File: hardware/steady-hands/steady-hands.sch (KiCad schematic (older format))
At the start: 16 parts, among them J1 SWD, J2 UART, J3 I2C, SW1 SW_Push, SW2 SW_SPDT, U1 STM32F411CEUx

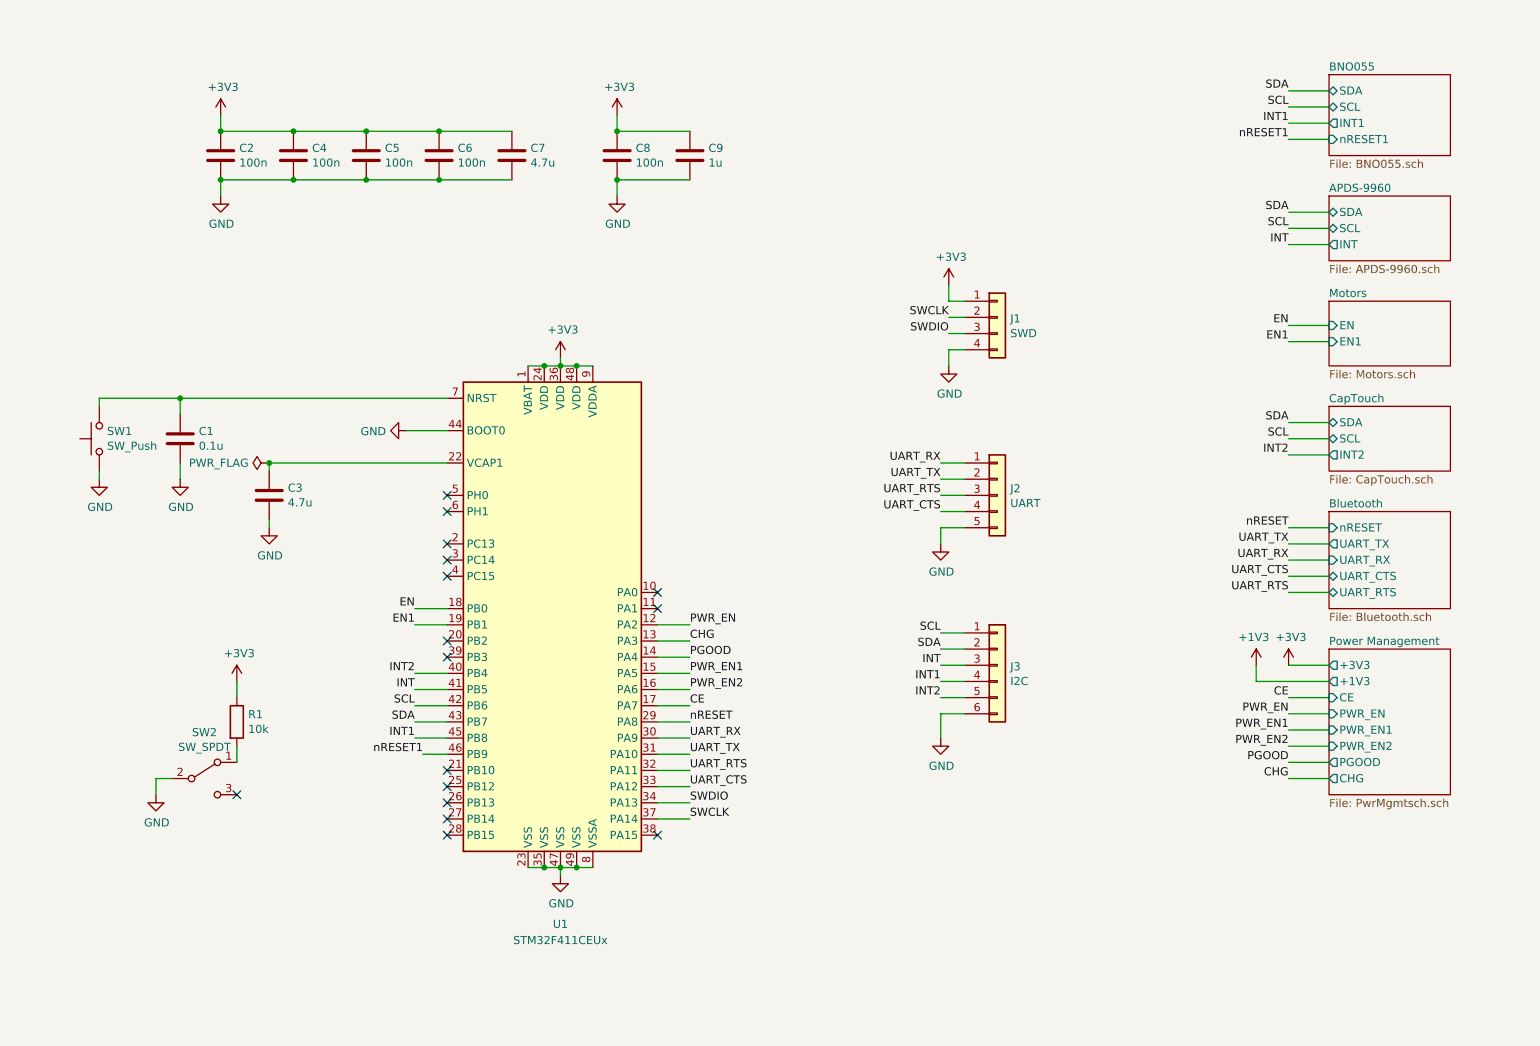
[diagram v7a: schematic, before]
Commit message: Edits label names and switch configuration
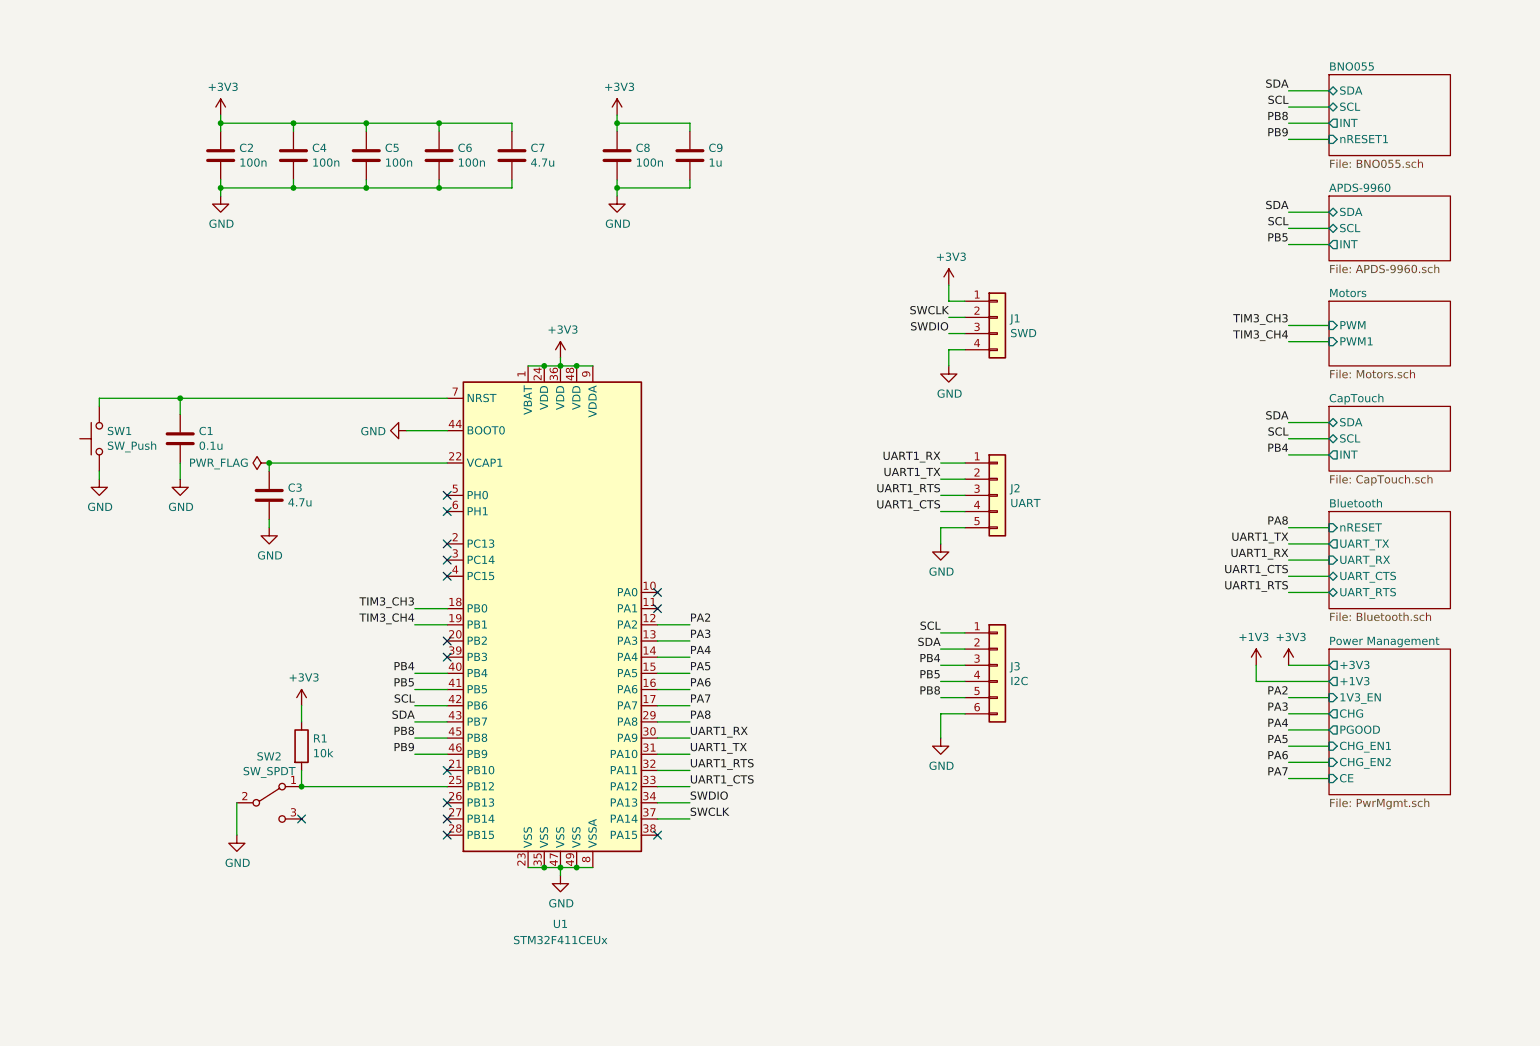
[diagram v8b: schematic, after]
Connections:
- net at U1.25 (PB12): now also R1.2, SW2.1 (A)
- net CE renamed PA7
- net CHG renamed PA3
- net EN renamed TIM3_CH3
- net EN1 renamed TIM3_CH4
- net INT renamed PB4
- net PB4: now also U1.40 (PB4); no longer U1.41 (PB5)
- net INT1 renamed PB5
- net PB5: now also U1.41 (PB5); no longer U1.45 (PB8)
- net INT2 renamed PB8
- net PB8: now also U1.45 (PB8); no longer U1.40 (PB4)
- net PGOOD renamed PA4
- net PWR_EN renamed PA2
- net PWR_EN1 renamed PA5
- net PWR_EN2 renamed PA6
- net UART_CTS renamed UART1_CTS
- net UART_RTS renamed UART1_RTS
- net UART_RX renamed UART1_RX
- net UART_TX renamed UART1_TX
- net nRESET renamed PA8
- net nRESET1 renamed PB9
- no-connect marks 16 -> 15
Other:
- moved on the sheet: R1, SW2
